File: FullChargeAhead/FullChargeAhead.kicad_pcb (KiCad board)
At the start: 2 copper layers, 0 parts

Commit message: Added new library and imported footprints
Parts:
- added C101: 4.7U, Capacitors_SMD:C_1206_HandSoldering, F.Cu at (169.8, 126.6)
- added C102: 4.7U, Capacitors_SMD:C_1206_HandSoldering, F.Cu at (187.2, 107.1)
- added CON101: USB-MICRO-B, FCA:10118193, F.Cu at (148.5, 105.5)
- added D101: NOPOP, LEDs:LED-0805, F.Cu at (153.1, 129.0)
- added D102: LED, LEDs:LED-0805, F.Cu at (162.7, 129.0)
- added D103: LED, LEDs:LED-0805, F.Cu at (158.2, 129.0)
- added P101: CONN_01X02, Pin_Headers:Pin_Header_Straight_1x02, F.Cu at (155.3, 122.0)
- added P102: CONN_01X02, Pin_Headers:Pin_Header_Straight_1x02, F.Cu at (168.8, 97.9)
- added R101: 470, Resistors_SMD:R_0805_HandSoldering, F.Cu at (193.5, 113.3)
- added R102: 470, Resistors_SMD:R_0805_HandSoldering, F.Cu at (195.4, 126.1)
- added R103: NOPOP, Resistors_SMD:R_0805_HandSoldering, F.Cu at (193.7, 106.9)
- added R104: 1K, Resistors_SMD:R_0805_HandSoldering, F.Cu at (176.1, 126.4)
- added R105: 10K, Resistors_SMD:R_0805_HandSoldering, F.Cu at (184.2, 117.8)
- added R106: 2K, Resistors_SMD:R_0805_HandSoldering, F.Cu at (184.2, 124.2)
- added R107: NOPOP, Resistors_SMD:R_0805_HandSoldering, F.Cu at (189.8, 119.7)
- added R108: NOPOP, Resistors_SMD:R_0805_HandSoldering, F.Cu at (189.8, 126.1)
- added R109: NOPOP, Resistors_SMD:R_0805_HandSoldering, F.Cu at (195.6, 119.7)
- added U101: MCP73834-FCI/UN, Housings_SSOP:MSOP-10_3x3mm_Pitch0.5mm, F.Cu at (173.9, 119.5)

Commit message: Halfway through layout, top planes poured
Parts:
- moved R109 62.5 mm to (137.9, 95.6)
- moved R108 62.5 mm to (132.1, 102.0)
- moved R107 62.5 mm to (132.1, 95.6)
- moved R102 38.5 mm to (159.4, 112.5), turned to 180 degrees
- moved R101 34.2 mm to (159.3, 116.0), turned to 180 degrees
- moved D101 30.9 mm to (181.5, 116.7), turned to 270 degrees
- moved C101 27.1 mm to (158.9, 101.8)
- moved CON101 24.5 mm to (125.3, 97.5)
- moved P101 20.1 mm to (175.0, 117.7), turned to 270 degrees
- moved D102 18.6 mm to (154.1, 112.5)
- moved R103 15.1 mm to (180.0, 113.2)
- moved R106 14.2 mm to (173.5, 114.8)
- moved D103 13.8 mm to (153.9, 115.9)
- moved P102 12.2 mm to (181.0, 98.5), turned to 270 degrees
- moved R104 9.69 mm to (178.6, 117.0), turned to 270 degrees
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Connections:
- net Net-(C101-Pad1) renamed /Vdd
- net Net-(C102-Pad1) renamed /Vbat
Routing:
- added copper zone on F.Cu, net /Vbat
- added copper zone on F.Cu, net /Vdd
- added copper zone on F.Cu, net GND

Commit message: Added planes and board outline, completed routing traces
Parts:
- moved CON101 27.2 mm to (152.6, 98.6), turned to 180 degrees
- moved R107 19.2 mm to (148.5, 105.5), turned to 90 degrees
- moved R108 19.1 mm to (151.0, 105.4), turned to 90 degrees
- moved R109 18.3 mm to (153.3, 105.5), turned to 90 degrees
- moved R105 14.5 mm to (176.7, 111.0), turned to 180 degrees
- moved D101 12.7 mm to (169.7, 121.4), turned to 0 degrees
- moved R101 5.10 mm to (156.0, 112.1)
- moved D103 4.73 mm to (151.1, 112.1)
- moved R102 4.18 mm to (156.0, 114.9)
- moved D102 3.97 mm to (151.1, 115.0)
- moved R103 3.87 mm to (181.0, 117.0), turned to 270 degrees
- moved C101 3.84 mm to (158.7, 105.6)
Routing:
- net /Vdd: track 0.00 -> 35.3 mm
- net GND: track 0.00 -> 17.8 mm, vias 0 -> 1
- net Net-(D101-Pad2): track 0.00 -> 12.5 mm
- net Net-(R103-Pad1): track 0.00 -> 11.8 mm
- net Net-(R102-Pad1): track 0.00 -> 11.8 mm
- net Net-(R101-Pad1): track 0.00 -> 10.9 mm
- net Net-(CON101-Pad4): track 0.00 -> 5.79 mm
- net Net-(R106-Pad2): track 0.00 -> 4.59 mm
- net Net-(P101-Pad1): track 0.00 -> 3.82 mm
- net Net-(CON101-Pad3): track 0.00 -> 3.42 mm
- net Net-(R105-Pad2): track 0.00 -> 3.18 mm
- net Net-(CON101-Pad2): track 0.00 -> 2.87 mm
- net Net-(D102-Pad2): track 0.00 -> 2.58 mm
- net Net-(D103-Pad2): track 0.00 -> 2.49 mm
- added copper zone on B.Cu, net /Vbat
- added copper zone on B.Cu, net /Vdd
- added copper zone on B.Cu, net GND
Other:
- board outline added: 45.4 x 25.5 mm
- net class Default: clearance 0.254 -> 0.1524; trace_width 0.254 -> 0.1524; via_dia 0.889 -> 0.6858; via_drill 0.635 -> 0.3302
- rule trace_clearance: 0.254 -> 0.1524
- rule trace_min: 0.254 -> 0.1524
- rule via_min_drill: 0.508 -> 0.3302
- rule via_min_size: 0.889 -> 0.6858

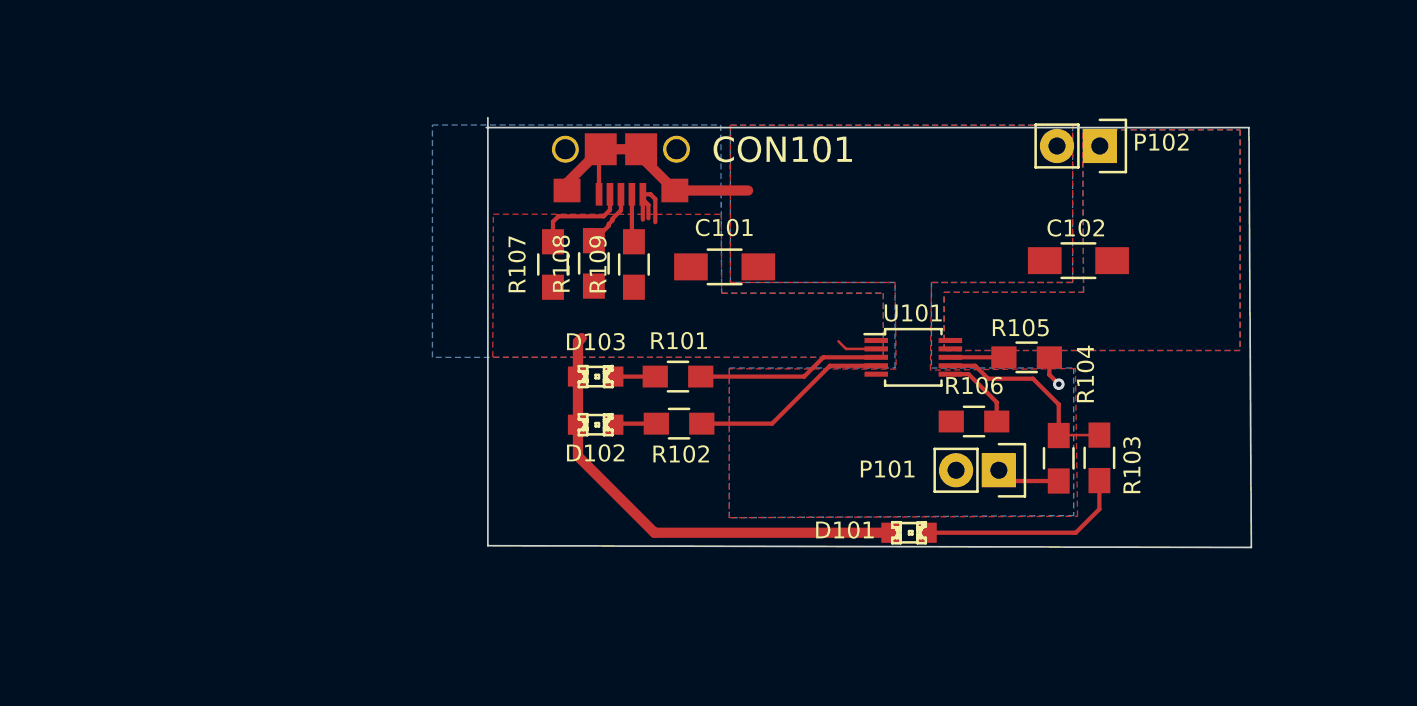
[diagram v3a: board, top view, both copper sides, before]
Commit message: Finished DRC and added title & silkscreen image
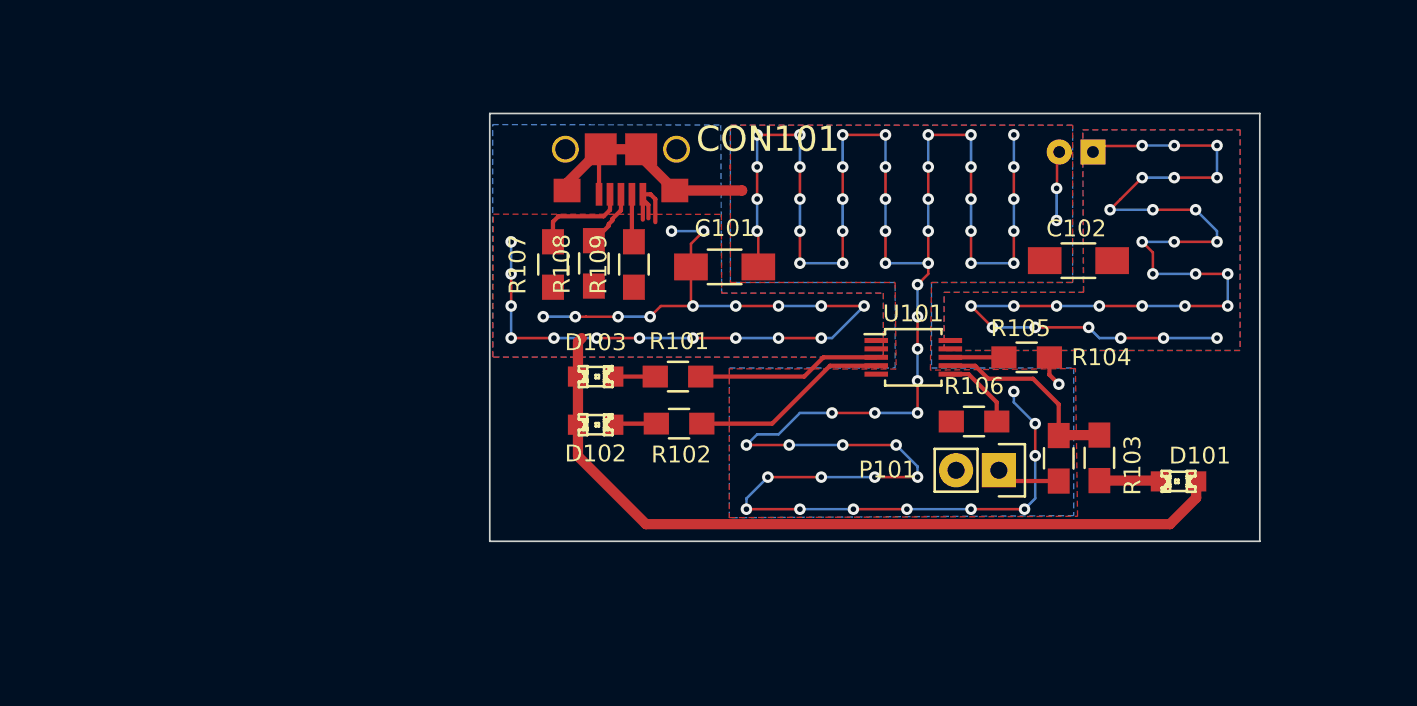
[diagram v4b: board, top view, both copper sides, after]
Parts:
- added G***: FCA-TINY, FCA:FCA-TINY, B.Cu at (168.1, 103.4)
- P102: footprint Pin_Headers:Pin_Header_Straight_1x02 -> FCA:JST_2pin; moved to B.Cu
- moved D101 16.3 mm to (185.7, 118.4), turned to 180 degrees
- moved P102 0.54 mm to (180.6, 98.8), turned to 90 degrees
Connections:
- R107 pad 1: GND -> /Vdd
- R108 pad 1: GND -> /Vdd
- R109 pad 1: GND -> /Vdd
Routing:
- net GND: track 17.8 -> 157.8 mm, vias 1 -> 61
- net /Vdd: track 35.3 -> 106.1 mm, vias 0 -> 22
- net /Vbat: track 0.00 -> 67.1 mm, vias 0 -> 28
- net Net-(D101-Pad2): track 12.5 -> 3.67 mm
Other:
- board size 45.4 x 25.5 mm -> 45.7 x 25.4 mm
- board text added: "Full Charge Ahead!"

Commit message: Change to R105 and generated final gerbers
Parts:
- R105: footprint Resistors_SMD:R_0805_HandSoldering -> Resistors_ThroughHole:Resistor_Horizontal_RM10mm
- moved R105 2.04 mm to (176.8, 109.0), turned to 315 degrees
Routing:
- net Net-(R105-Pad2): track 3.18 -> 8.94 mm
- net GND: track 157.8 -> 156.0 mm, vias 61 -> 59
